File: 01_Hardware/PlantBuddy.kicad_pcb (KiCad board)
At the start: 2 copper layers, 35 x 87.3 mm, 42 parts, among them J1 SWD+DBG, J2 Conn_I2C_SDA, J3 Conn_I2C_SCL, Q1 AO3401, Q2 AO3400A, U1 OPT3001, U2 nRF52810-QCxx, U3 LMC555xM, U6 SHTC3, Y1 32MHz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

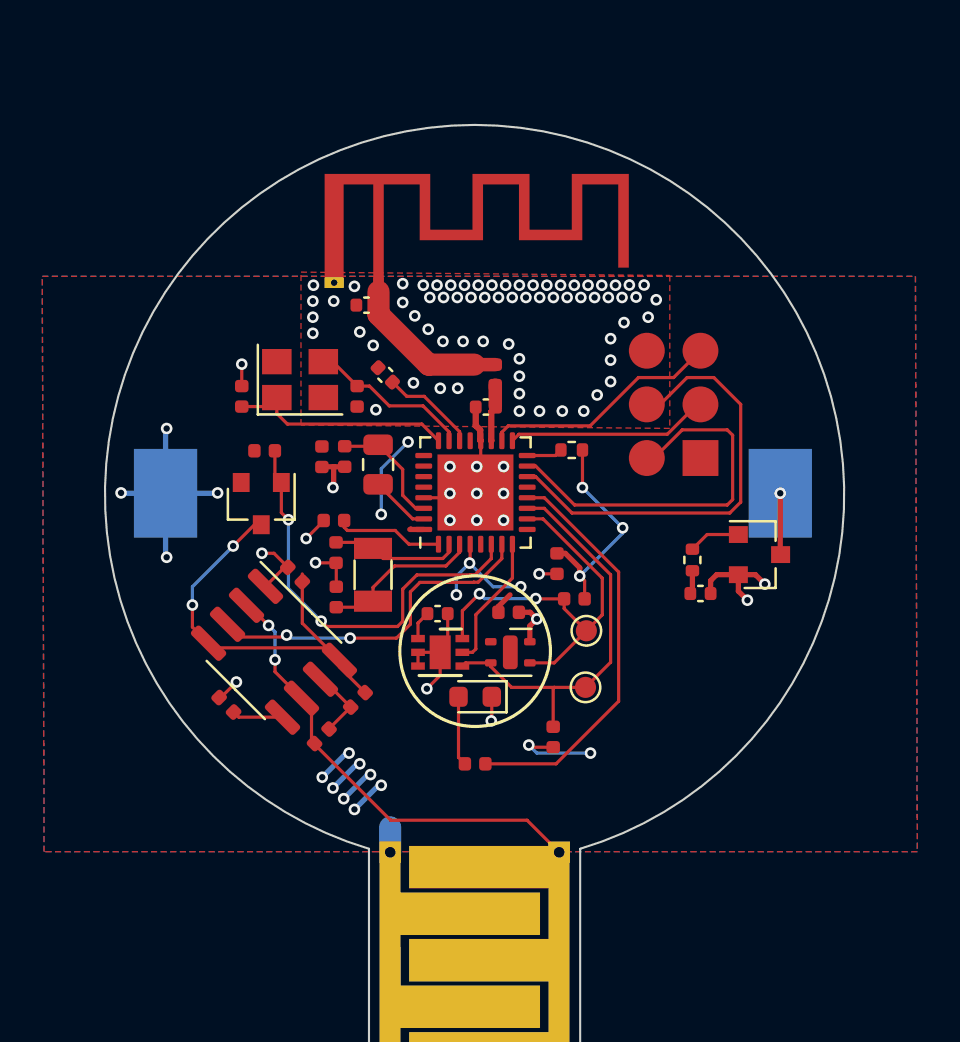
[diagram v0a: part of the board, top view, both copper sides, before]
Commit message: PlantBuddy Revision 3. Switched to nRF52832
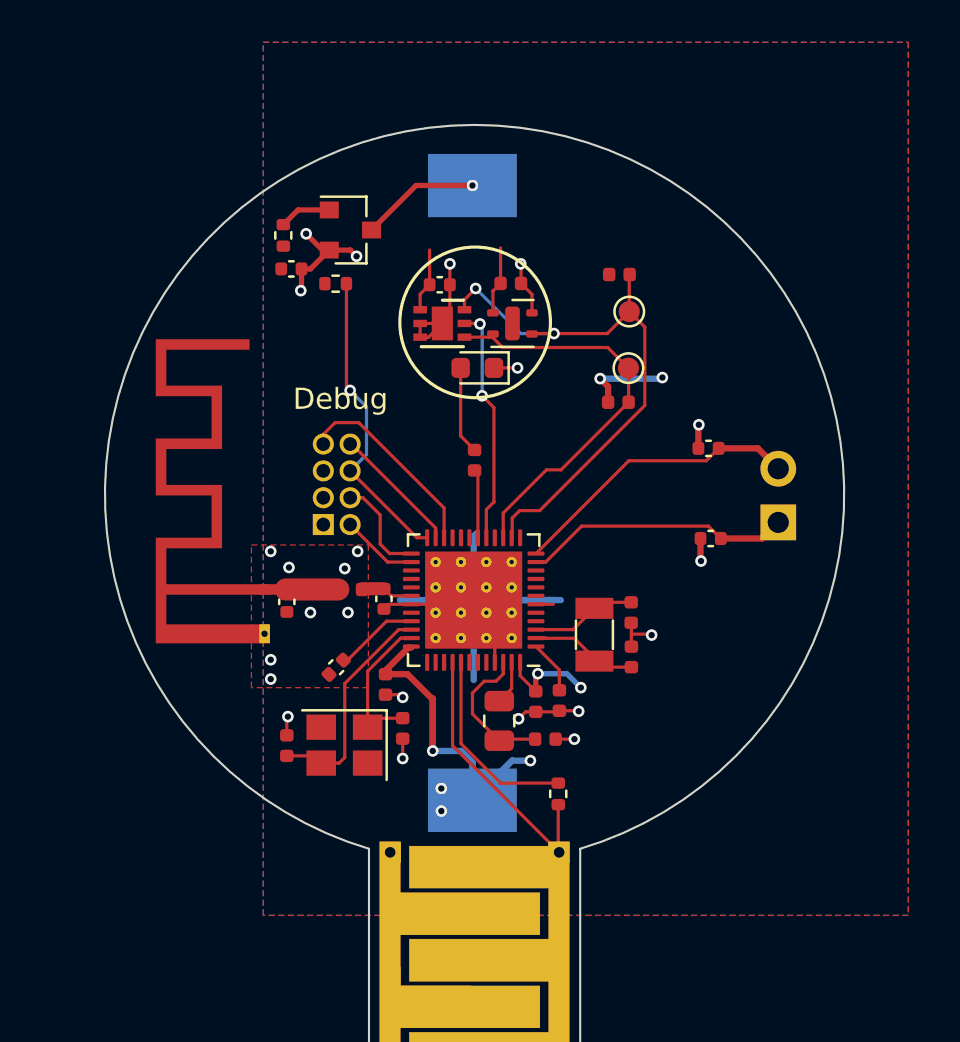
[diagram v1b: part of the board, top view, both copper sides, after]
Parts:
- removed C1, C2: 100nF, Capacitor_SMD:C_0402_1005Metric
- removed J1: SWD+DBG, Connector_PinHeader_2.54mm:PinHeader_2x03_P2.54mm_Vertical
- removed Q1: AO3401, Package_TO_SOT_SMD:SOT-23
- removed R2, R8, R9: 10k, Resistor_SMD:R_0402_1005Metric
- removed U2: nRF52810-QCxx, Package_DFN_QFN:QFN-32-1EP_5x5mm_P0.5mm_EP3.6x3.6mm
- removed U3: LMC555xM, Package_SO:SOIC-8_3.9x4.9mm_P1.27mm
- added C101: N/P, Capacitor_SMD:C_0402_1005Metric, F.Cu at (76.9, 66.5)
- added C102: N/P, Capacitor_SMD:C_0402_1005Metric, F.Cu at (76.8, 62.2)
- added J101: Debug, PlantBuddy:PinHeader_2x04_P1.27mm_Vertical, B.Cu at (58.6, 65.9)
- added J102: NFC Antenna, Connector_PinHeader_2.54mm:PinHeader_1x02_P2.54mm_Vertical, B.Cu at (80.1, 65.8)
- added R101: 100k, Resistor_SMD:R_0402_1005Metric, F.Cu at (69.7, 78.6)
- added U101: nRF52832-QFxx, Package_DFN_QFN:QFN-48-1EP_6x6mm_P0.4mm_EP4.6x4.6mm_ThermalVias, F.Cu at (65.7, 69.4)
- moved R4 24.7 mm to (56.7, 52.2)
- moved C15 24.7 mm to (57.0, 53.7)
- moved Q2 24.7 mm to (59.8, 51.9)
- moved C6 17.5 mm to (62.3, 75.5), turned to 90 degrees
- moved Y1 17.4 mm to (59.6, 76.3), turned to 180 degrees
- moved C11 16.9 mm to (56.8, 76.3), turned to 270 degrees
- moved C16 16.4 mm to (69.1, 76.0), turned to 180 degrees
- moved R14 16.1 mm to (72.5, 60.1), turned to 0 degrees
- moved U1 15.6 mm to (64.2, 56.3)
- moved U6 15.6 mm to (67.5, 56.3)
- moved C17 15.6 mm to (64.1, 54.5)
- moved C3 15.6 mm to (67.4, 54.4)
- moved D1 15.6 mm to (65.8, 58.4)
- moved R15 15.5 mm to (72.6, 54.0), turned to 0 degrees
- moved AE1 15.5 mm to (55.8, 68.9), turned to 90 degrees
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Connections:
- C4 pad 1: /THR -> /Discharge
- R1 pad 2: Net-(R1-Pad2) -> /~RST
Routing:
- net /THR: track 21.6 -> 0.00 mm, vias 2 -> 0
- net Net-(C1-Pad1): track 20.8 -> 0.00 mm, vias 2 -> 0
- net /~SOIL_EN~: track 20.0 -> 0.00 mm, vias 2 -> 0
- net GND: track 33.2 -> 52.4 mm, vias 88 -> 23
- net /fHumidity: track 16.5 -> 0.00 mm, vias 2 -> 0
- net /LEDY: track 19.4 -> 3.25 mm
- net /UART_Tx: track 21.2 -> 6.16 mm
- net /~RST: track 0.00 -> 14.5 mm, vias 0 -> 1
- net Net-(C102-Pad1): track 0.00 -> 13.9 mm
- net +BATT: track 46.9 -> 33.5 mm, vias 22 -> 8
- net /Discharge: track 0.00 -> 13.4 mm
- net Net-(C101-Pad2): track 0.00 -> 12.7 mm
- net /UART_Rx: track 18.9 -> 9.49 mm
- net /Charge: track 0.00 -> 9.23 mm
- net /SWDIO: track 11.4 -> 3.63 mm
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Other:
- board text added: "Debug"
- board text added: "NFC"
- board text added: "PlantBuddy"
- board text added: "by Ardelean Calin & Geanina Toader"
- board text removed: "FlivzNexxy"

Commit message: HW: Rev 4.1 => Changed ALS from OPT3001 to LTR-303
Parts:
- removed U1: OPT3001, Package_DFN_QFN:DFN-6-1EP_2x2mm_P0.65mm_EP1x1.6mm
- added U102: LTR-303ALS-01, OptoDevice:Lite-On_LTR-303ALS-01, F.Cu at (64.0, 56.3)
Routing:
- net GND: track 52.4 -> 50.7 mm

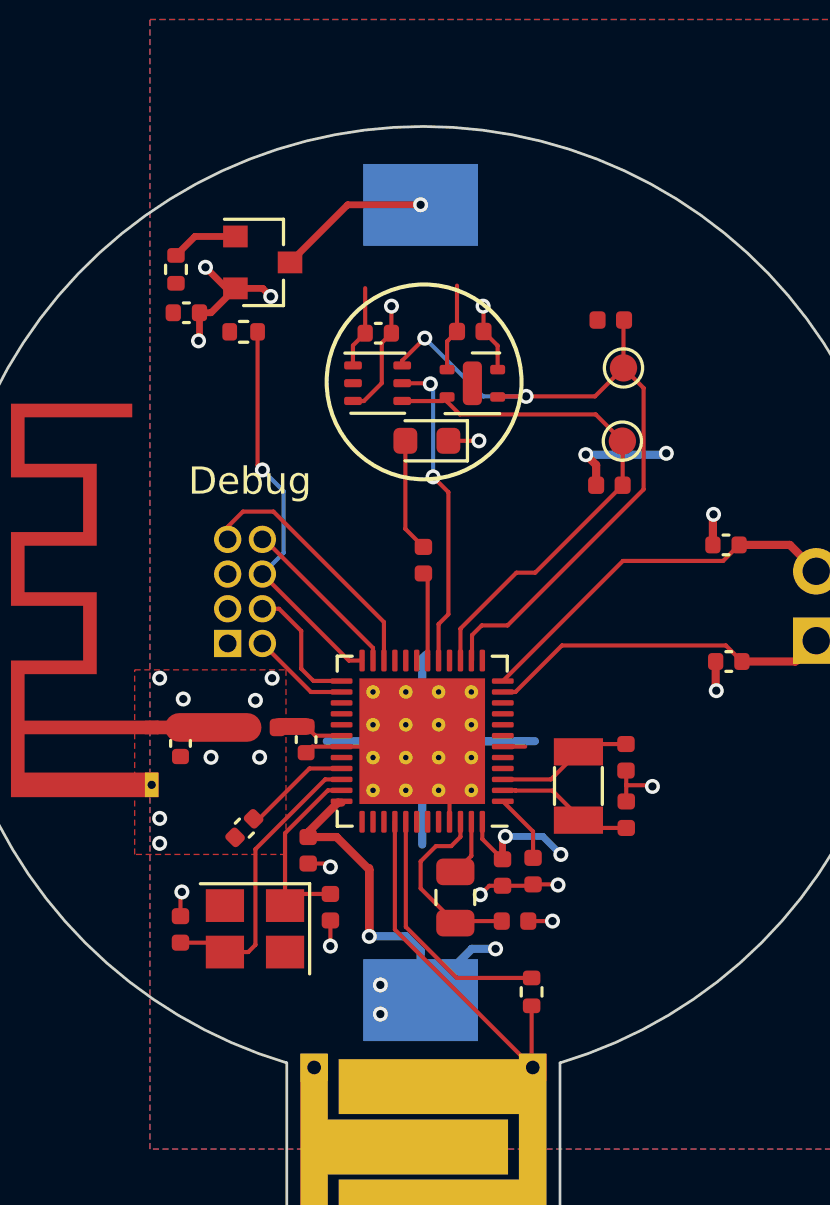
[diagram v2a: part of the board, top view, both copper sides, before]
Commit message: Started PCB improvements & added SVGs and interactive BOM.
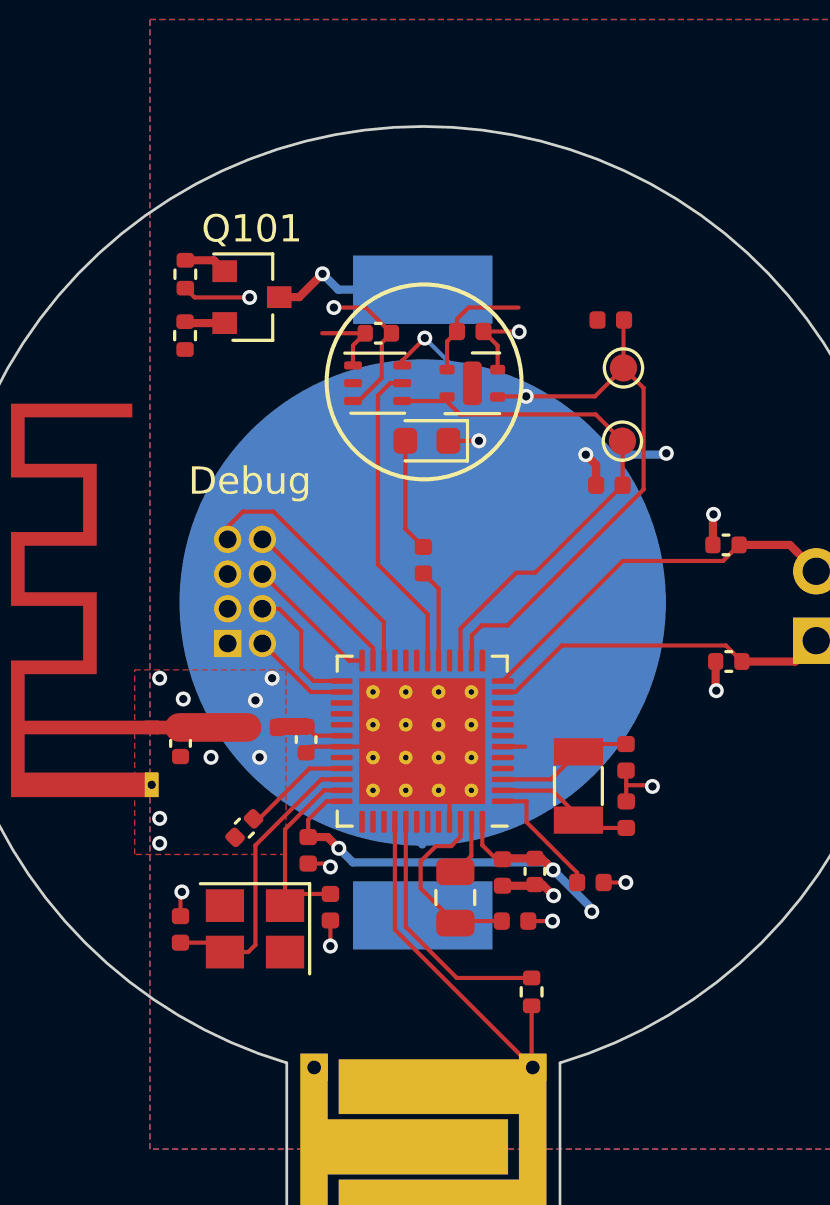
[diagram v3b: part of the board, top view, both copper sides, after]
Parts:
- removed Q2: AO3400A, Package_TO_SOT_SMD:SOT-23
- added Q101: AO3401A, Package_TO_SOT_SMD:SOT-23, F.Cu at (59.4, 53.2)
- BT1: footprint PlantBuddy:BatteryHolder_LCSC_2032 -> PlantBuddy:BAT-HLD-001
- C15: value 4.7uF -> 1uF
- moved C15 24.1 mm to (69.8, 74.2), turned to 270 degrees
- moved BT1 13.8 mm to (57.9, 75.8)
- moved R1 2.15 mm to (57.0, 54.6), turned to 270 degrees
- moved C5 2.14 mm to (71.8, 74.6), turned to 180 degrees
- moved R4 0.39 mm to (57.0, 52.3), turned to 270 degrees
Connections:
- BT1 pad 1: +BATT -> Net-(BT1-Pad1)
- BT1 pad 2: Net-(BT1-Pad2) -> GND
- R4 pad 1: +BATT -> Net-(Q101-Pad1)
- R4 pad 2: Net-(Q2-Pad1) -> GND
- U101 pad 17: /LUX_INT -> /LEDY
- U101 pad 18: /LEDY -> /LUX_INT
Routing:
- net /~RST: track 14.5 -> 4.96 mm, vias 1 -> 0
- net Net-(BT1-Pad1): track 0.00 -> 5.84 mm, vias 0 -> 1
- net Net-(BT1-Pad2): track 5.66 -> 0.00 mm, vias 1 -> 0
- net Net-(Q2-Pad1): track 2.46 -> 0.00 mm
- net Net-(C5-Pad2): track 2.53 -> 4.61 mm
- net +BATT: track 33.5 -> 31.8 mm, vias 8 -> 5
- net Net-(Q101-Pad1): track 0.00 -> 1.60 mm
- net GND: track 50.7 -> 49.2 mm, vias 23 -> 21
- net /LUX_INT: track 11.3 -> 11.5 mm, vias 2 -> 0

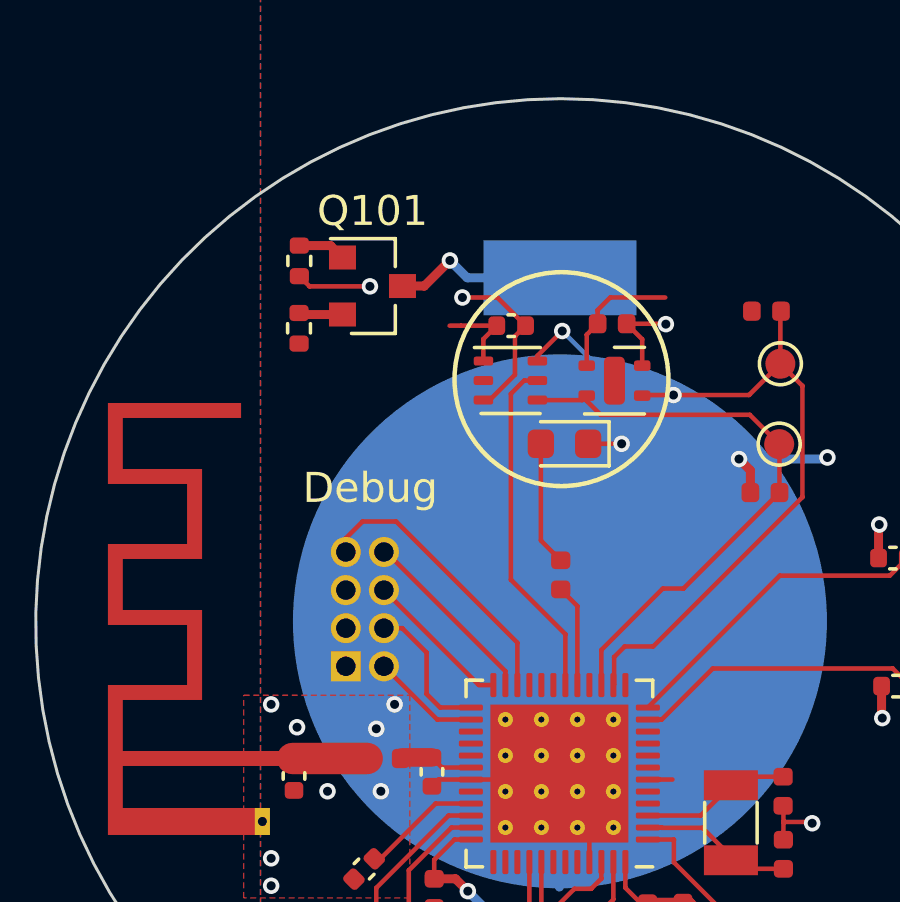
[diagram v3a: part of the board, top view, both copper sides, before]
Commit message: Added new debug connector for J-Link.
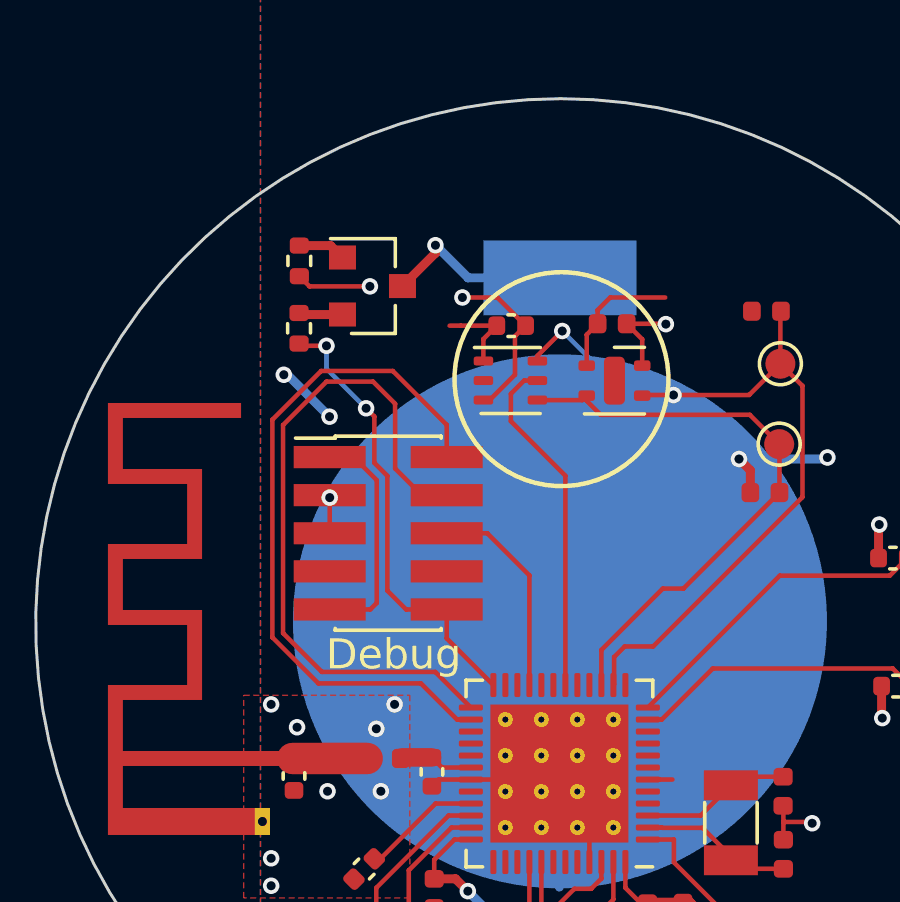
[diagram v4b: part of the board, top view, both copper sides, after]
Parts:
- removed D1: Y, LED_SMD:LED_0603_1608Metric
- removed G***: LOGO, PlantBuddy:qr
- removed R3: 1k, Resistor_SMD:R_0402_1005Metric
- J101: value Debug -> J-Link SWD; footprint PlantBuddy:PinHeader_2x04_P1.27mm_Vertical -> Connector_PinHeader_1.27mm:PinHeader_2x05_P1.27mm_Vertical_SMD; moved to F.Cu
- moved J101 4.65 mm to (60.0, 61.4)
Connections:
- J101 pad 6: /~RST -> /SWO
- J101 pad 7: /UART_Rx -> Net-(J101-Pad7)
- J101 pad 8: /UART_Tx -> Net-(J101-Pad8)
- U101 pad 17: /LEDY -> /SPEAKER
- U101 pad 21: Net-(U101-Pad21) -> /SWO
- U101 pad 22: /UART_Rx -> Net-(U101-Pad22)
- U101 pad 23: /UART_Tx -> Net-(U101-Pad23)
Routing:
- net /SWDIO: track 3.63 -> 23.3 mm
- net /SWCLK: track 4.80 -> 23.1 mm
- net /~RST: track 4.96 -> 15.4 mm, vias 0 -> 2
- net +BATT: track 31.8 -> 41.6 mm, vias 5 -> 7
- net /UART_Rx: track 9.49 -> 0.00 mm
- net /SWO: track 0.00 -> 6.99 mm
- net /UART_Tx: track 6.16 -> 0.00 mm
- net Net-(D1-Pad2): track 4.16 -> 0.00 mm
- net /LEDY: track 3.42 -> 0.00 mm
- net Net-(BT1-Pad1): track 5.84 -> 6.42 mm

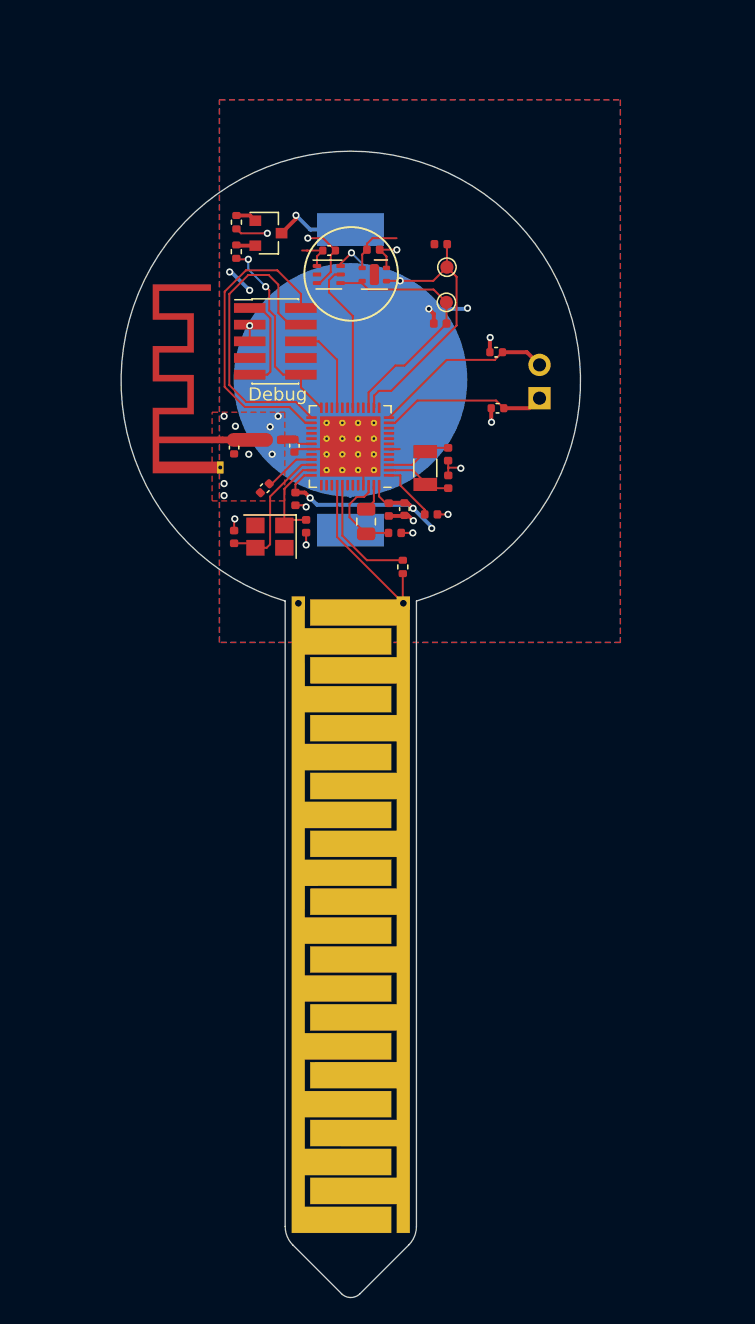
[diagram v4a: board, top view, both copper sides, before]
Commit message: Changed antenna design to monopole
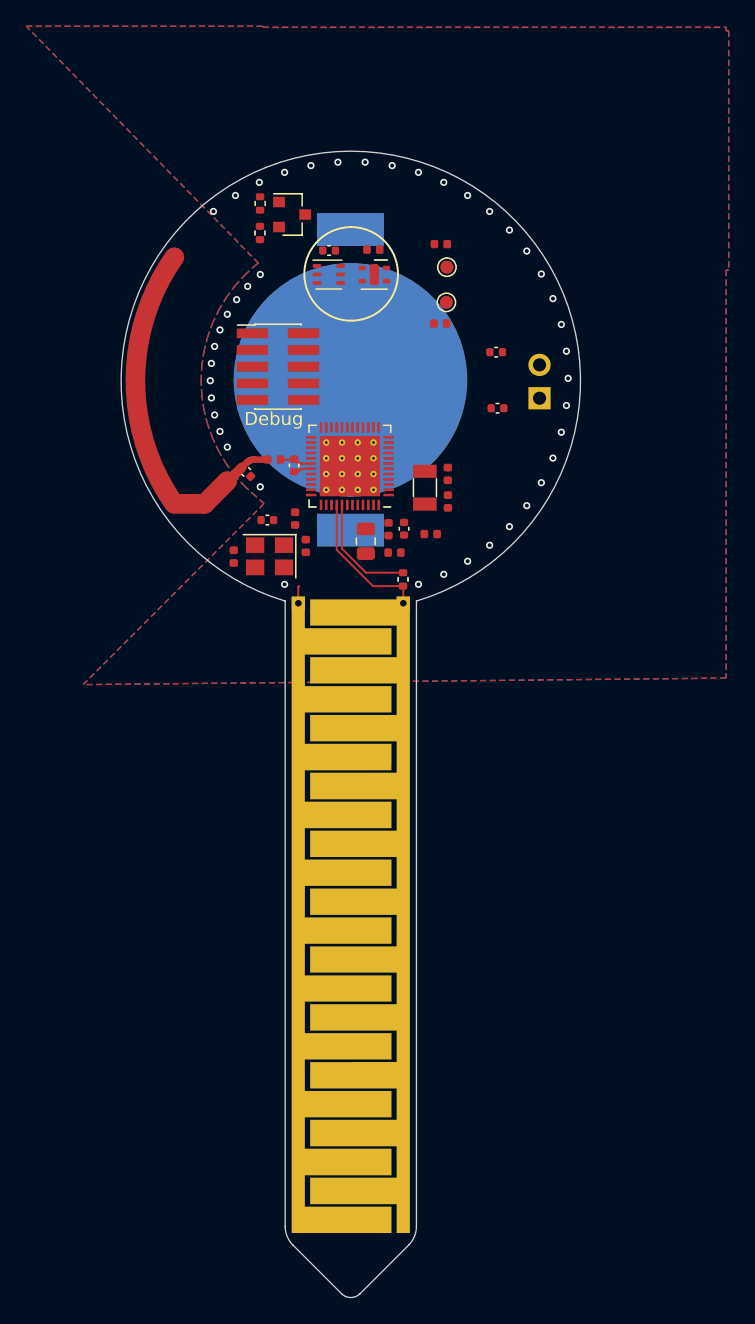
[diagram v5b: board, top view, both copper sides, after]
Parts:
- removed AE1: 2.45GHz PCB antenna, RF_Antenna:Texas_SWRA117D_2.4GHz_Right
- added AE101: Antenna, PlantBuddy:monopole, F.Cu at (65.7, 64.4)
- moved C9 2.43 mm to (59.4, 75.0), turned to 0 degrees
- moved R1 2.30 mm to (58.8, 53.2)
- moved Q101 2.30 mm to (61.2, 51.8)
- moved R4 2.30 mm to (58.8, 50.9)
- moved C7 2.07 mm to (57.8, 71.4), turned to 315 degrees
- moved J101 1.94 mm to (60.2, 63.3)
- moved C12 1.50 mm to (68.6, 75.7)
- moved C13 1.50 mm to (73.1, 71.5)
- moved L4 1.50 mm to (66.9, 76.6)
- moved C10 1.50 mm to (61.5, 74.9)
- moved C11 1.50 mm to (56.8, 77.8)
- moved C15 1.50 mm to (69.8, 75.7)
- moved C16 1.50 mm to (69.0, 77.5)
- moved C6 1.50 mm to (62.3, 77.0)
- moved C8 1.50 mm to (61.4, 70.9)
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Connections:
- net /Discharge renamed /Measure
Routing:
- net GND: track 49.4 -> 2.71 mm, vias 21 -> 43
- net +BATT: track 41.6 -> 0.00 mm, vias 7 -> 0
- net /SDA: track 26.9 -> 0.00 mm, vias 2 -> 0
- net /SWDIO: track 23.3 -> 0.00 mm
- net /SWCLK: track 23.1 -> 0.00 mm
- net /SCL: track 19.5 -> 0.00 mm
- net /~RST: track 15.4 -> 0.00 mm, vias 2 -> 0
- net Net-(C102-Pad1): track 13.9 -> 0.00 mm
- net Net-(C101-Pad2): track 12.7 -> 0.00 mm
- net /LUX_INT: track 11.5 -> 0.00 mm
- net /XC1: track 10.8 -> 0.00 mm
- net /XC2: track 7.29 -> 0.00 mm
- net /SWO: track 6.99 -> 0.00 mm
- net Net-(C16-Pad2): track 6.90 -> 0.00 mm
- net Net-(BT1-Pad1): track 6.42 -> 0.00 mm, vias 1 -> 0
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- removed copper zone on F.Cu, net +BATT
